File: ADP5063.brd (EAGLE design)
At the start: 33 x 14.9 mm, 23 parts, among them X1 PIIKKIRIMA-5, X2 PIIKKIRIMA-5, X3 PIIKKIRIMA-5, X4 PIIKKIRIMA-5, X5 629105136821

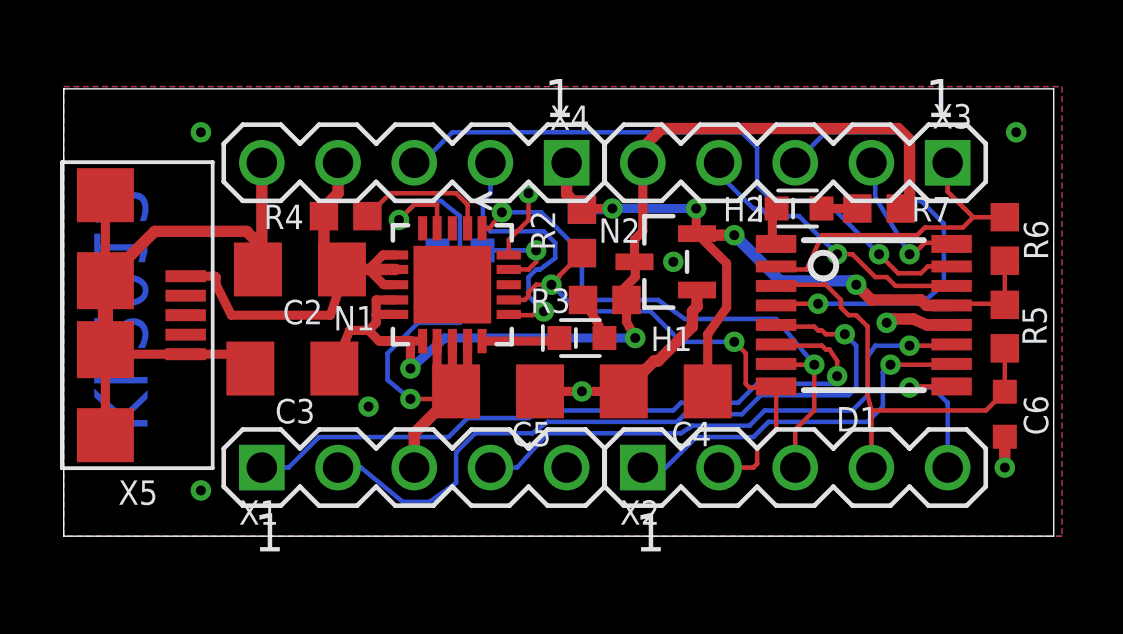
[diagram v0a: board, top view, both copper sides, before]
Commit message: VCC/GND Fixed
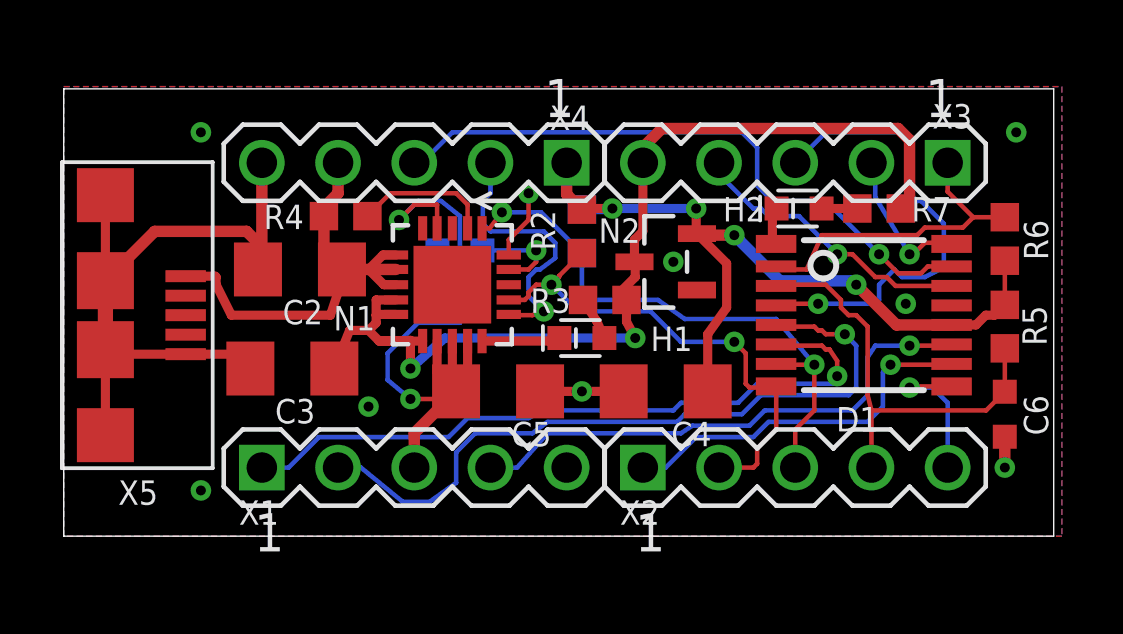
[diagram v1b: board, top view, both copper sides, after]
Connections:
- net +3V3: now also D1.12; no longer D1.13
- net GND: now also D1.13; no longer D1.12
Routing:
- net GND: track 36.5 -> 29.8 mm
- net +3V3: track 26.1 -> 26.6 mm
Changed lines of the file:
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@@
 <setting verticaltext="up"/>
 </settings>
-<grid distance="0.01" unitdist="inch" unit="inch" style="lines" multiple="1" display="no" altdistance="0.025" altunitdist="inch" altunit="inch"/>
+<grid distance="0.005" unitdist="inch" unit="inch" style="lines" multiple="1" display="no" altdistance="0.025" altunitdist="inch" altunit="inch"/>
 <layers>
 <layer number="1" name="Top" color="7" fill="1" visible="yes" active="yes"/>
@@
 <wire x1="34.016" y1="15.164" x2="1.016" y2="15.164" width="0" layer="20"/>
 <wire x1="1.016" y1="15.164" x2="1.016" y2="0.254" width="0" layer="20"/>
-<text x="3.81" y="11.938" size="1.778" layer="16" rot="MR270">KL2013</text>
+<text x="3.937" y="12.7" size="1.778" layer="30" font="vector" rot="MR270">KL2013</text>
 </plain>
 <attributes>
@@
 <contactref element="N2" pad="2"/>
 <contactref element="C4" pad="1"/>
-<contactref element="D1" pad="13"/>
 <contactref element="R2" pad="2"/>
 <contactref element="R1" pad="2"/>
@@
 <wire x1="22.098" y1="10.3632" x2="22.1234" y2="10.3378" width="0.3048" layer="1"/>
 <wire x1="32.385" y1="9.435" x2="32.385" y2="7.964" width="0.1524" layer="1"/>
-<wire x1="30.611" y1="7.945" x2="30.678" y2="7.945" width="0.1524" layer="1"/>
-<wire x1="30.678" y1="7.945" x2="30.734" y2="8.001" width="0.1524" layer="1"/>
-<wire x1="30.734" y1="8.001" x2="32.348" y2="8.001" width="0.1524" layer="1"/>
-<wire x1="32.348" y1="8.001" x2="32.385" y2="7.964" width="0.1524" layer="1"/>
 <wire x1="17.78" y1="12.7" x2="17.78" y2="11.647" width="0.381" layer="1"/>
 <wire x1="17.78" y1="11.647" x2="18.288" y2="11.139" width="0.381" layer="1"/>
-<wire x1="30.611" y1="7.945" x2="29.774" y2="7.945" width="0.381" layer="1"/>
-<wire x1="29.774" y1="7.945" x2="29.591" y2="8.128" width="0.381" layer="1"/>
-<wire x1="29.591" y1="8.128" x2="27.94" y2="8.128" width="0.381" layer="1"/>
-<wire x1="27.94" y1="8.128" x2="27.432" y2="8.636" width="0.381" layer="1"/>
 <via x="27.432" y="8.636" extent="1-16" drill="0.3302"/>
 <wire x1="27.432" y1="8.636" x2="27.305" y2="8.763" width="0.381" layer="16"/>
@@
 <wire x1="23.368" y1="10.287" x2="22.1742" y2="10.287" width="0.381" layer="1"/>
 <wire x1="22.1742" y1="10.287" x2="22.1234" y2="10.3378" width="0.381" layer="1"/>
+<contactref element="D1" pad="12"/>
+<wire x1="30.611" y1="7.295" x2="28.773" y2="7.295" width="0.381" layer="1"/>
+<wire x1="28.773" y1="7.295" x2="27.432" y2="8.636" width="0.381" layer="1"/>
+<wire x1="30.611" y1="7.295" x2="31.425" y2="7.295" width="0.3048" layer="1"/>
+<wire x1="31.425" y1="7.295" x2="31.75" y2="7.62" width="0.3048" layer="1"/>
+<wire x1="31.75" y1="7.62" x2="32.041" y2="7.62" width="0.3048" layer="1"/>
+<wire x1="32.041" y1="7.62" x2="32.385" y2="7.964" width="0.3048" layer="1"/>
 </signal>
 <signal name="GND">
-<contactref element="D1" pad="12"/>
 <contactref element="N2" pad="1"/>
 <contactref element="C1" pad="2"/>
@@
 <wire x1="16.51" y1="10.795" x2="16.51" y2="11.684" width="0.1524" layer="1"/>
 <via x="16.51" y="11.684" extent="1-16" drill="0.3302"/>
-<wire x1="22.1234" y1="8.4582" x2="22.1234" y2="7.8994" width="0.381" layer="1"/>
-<wire x1="22.1234" y1="7.8994" x2="21.971" y2="7.747" width="0.381" layer="1"/>
-<wire x1="21.971" y1="7.747" x2="21.971" y2="7.239" width="0.381" layer="1"/>
-<wire x1="21.971" y1="7.239" x2="20.828" y2="6.096" width="0.381" layer="1"/>
-<wire x1="20.828" y1="6.096" x2="20.698" y2="6.096" width="0.381" layer="1"/>
-<wire x1="20.698" y1="6.096" x2="19.682" y2="5.08" width="0.381" layer="1"/>
-<wire x1="30.611" y1="7.295" x2="29.789" y2="7.295" width="0.381" layer="1"/>
-<wire x1="29.789" y1="7.295" x2="29.337" y2="7.493" width="0.381" layer="1"/>
-<wire x1="29.337" y1="7.493" x2="28.575" y2="7.493" width="0.381" layer="1"/>
-<wire x1="28.575" y1="7.493" x2="28.448" y2="7.366" width="0.381" layer="1"/>
-<via x="28.448" y="7.366" extent="1-16" drill="0.3302"/>
 <wire x1="32.385" y1="3.568" x2="32.385" y2="2.54" width="0.381" layer="1"/>
 <via x="32.385" y="2.54" extent="1-16" drill="0.3302"/>
@@
 <via x="5.588" y="13.716" extent="1-16" drill="0.3302"/>
 <via x="32.766" y="13.716" extent="1-16" drill="0.3302"/>
+<contactref element="D1" pad="13"/>
+<via x="29.083" y="8.001" extent="1-16" drill="0.3302"/>
 </signal>
 <signal name="VIN">
@@
 <wire x1="26.162" y1="8.001" x2="24.817" y2="8.001" width="0.1524" layer="1"/>
 <wire x1="24.817" y1="8.001" x2="24.761" y2="7.945" width="0.1524" layer="1"/>
-<wire x1="26.162" y1="8.001" x2="29.591" y2="8.001" width="0.1524" layer="16"/>
-<wire x1="29.591" y1="8.001" x2="30.353" y2="8.636" width="0.1524" layer="16"/>
-<wire x1="30.353" y1="8.636" x2="30.353" y2="10.668" width="0.1524" layer="16"/>
+<wire x1="26.162" y1="8.001" x2="28.067" y2="8.001" width="0.1524" layer="16"/>
+<wire x1="28.067" y1="8.001" x2="28.194" y2="8.128" width="0.1524" layer="16"/>
+<wire x1="28.194" y1="8.128" x2="28.194" y2="8.636" width="0.1524" layer="16"/>
+<wire x1="28.194" y1="8.636" x2="28.702" y2="9.144" width="0.1524" layer="16"/>
+<wire x1="28.702" y1="9.144" x2="28.956" y2="8.89" width="0.1524" layer="16"/>
+<wire x1="28.956" y1="8.89" x2="29.718" y2="8.89" width="0.1524" layer="16"/>
+<wire x1="29.718" y1="8.89" x2="30.226" y2="9.144" width="0.1524" layer="16"/>
+<wire x1="30.226" y1="9.144" x2="30.353" y2="9.398" width="0.1524" layer="16"/>
+<wire x1="30.353" y1="9.398" x2="30.353" y2="10.668" width="0.1524" layer="16"/>
 <wire x1="30.353" y1="10.668" x2="29.591" y2="11.43" width="0.1524" layer="16"/>
 <wire x1="29.591" y1="11.43" x2="29.464" y2="11.43" width="0.1524" layer="16"/>

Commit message: Added avatar
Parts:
- added U$1: (no value), dafug:DAFUG-.SM
